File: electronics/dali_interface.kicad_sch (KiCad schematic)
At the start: 34 parts, among them J1 Screw_Terminal_01x04, J4 Conn_01x02, Q1 MMBT5551L, Q2 DMN62D0U, U2 TPS62932

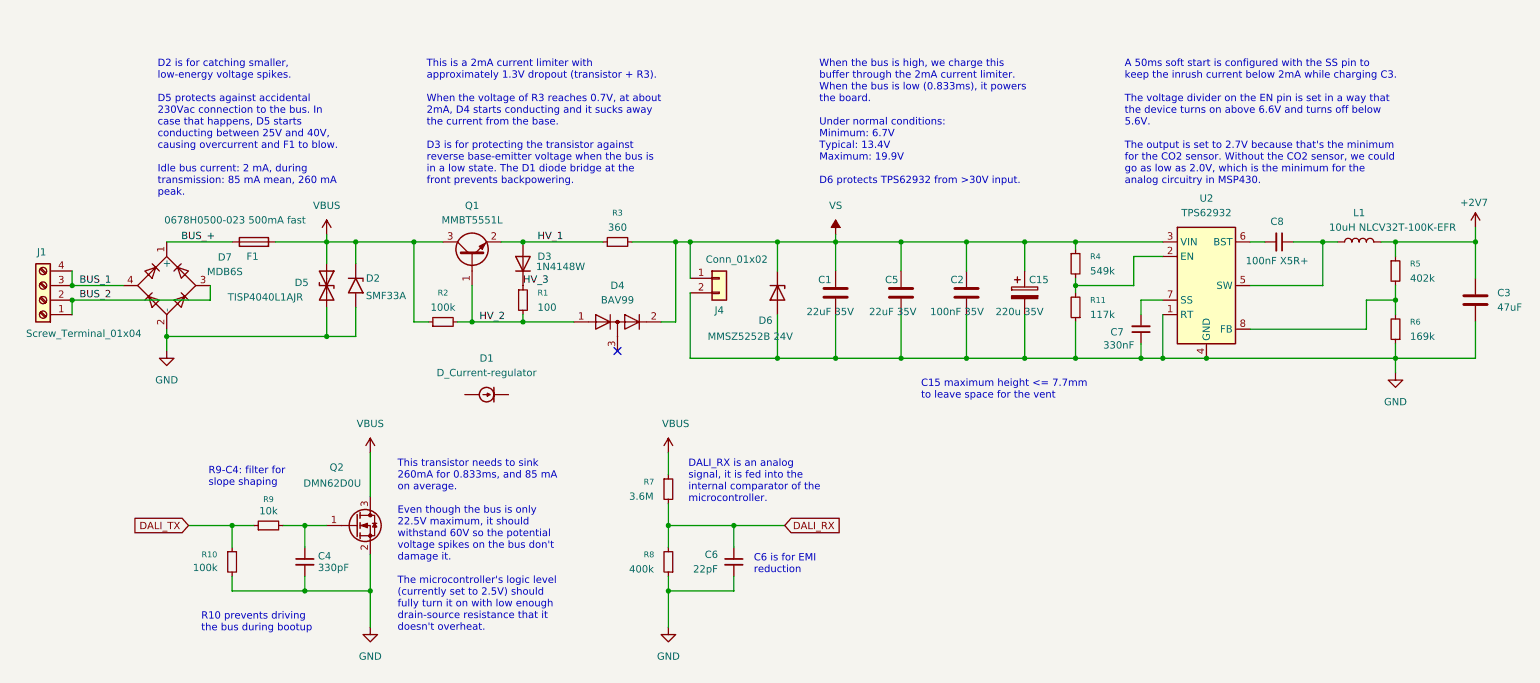
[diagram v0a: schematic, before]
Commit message: Fixed errors of the first hw prototype
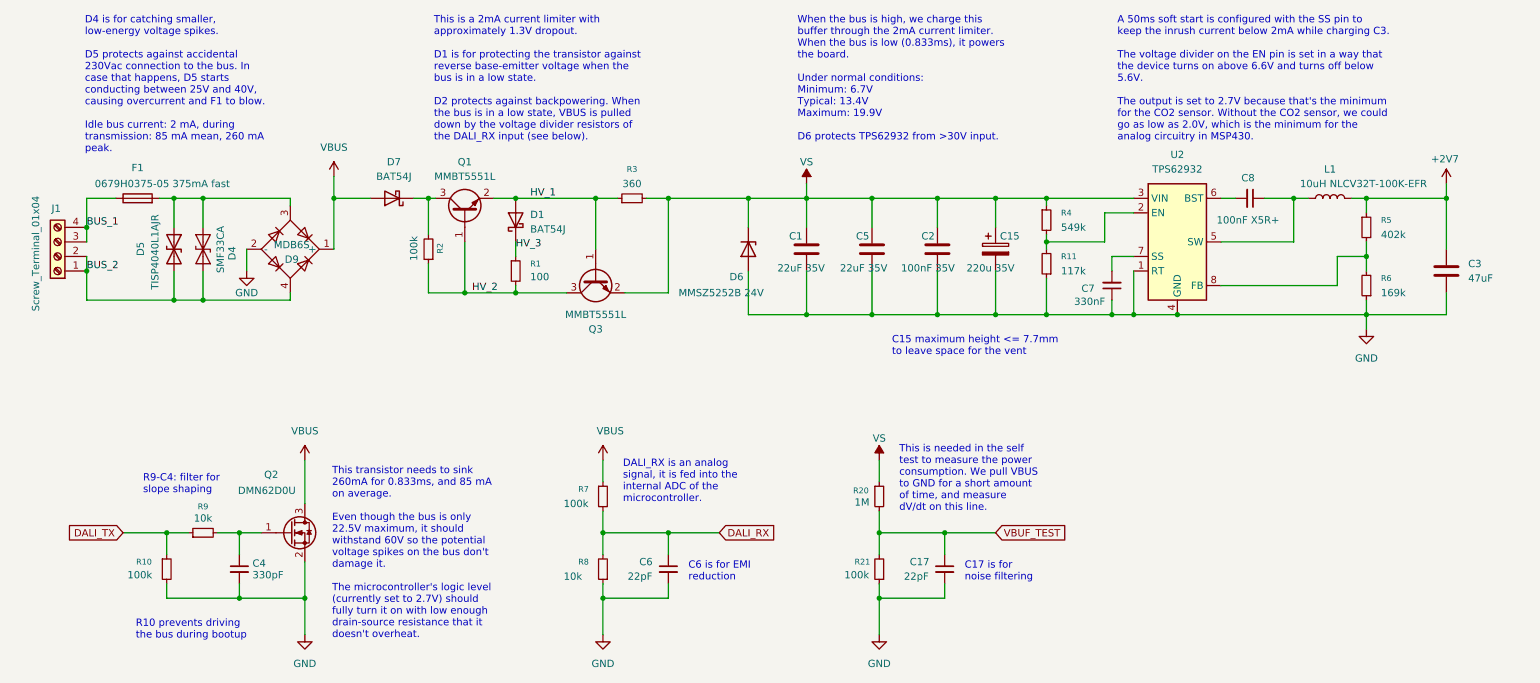
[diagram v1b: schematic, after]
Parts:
- removed D1: D_Current-regulator, Diode_SMD:D_MELF, symbol Device:D_Current-regulator
- removed D2: SMF33A, Diode_SMD:D_SMF-DEBUG, symbol Diode:SMF33A
- removed D3: 1N4148W, Diode_SMD:D_SOD-123, symbol Diode:1N4148W
- removed D4: BAV99, Package_TO_SOT_SMD:SOT-23, symbol Diode:BAV99
- removed D7: MDB6S, Package_SO:TSSOP-4_4.4x5mm_P4mm, symbol Diode_Bridge:MDB6S
- removed J4: Conn_01x02, Connector_PinSocket_1.27mm:PinSocket_1x02_P1.27mm_Vertical, symbol Connector_Generic:Conn_01x02
- added C17: 22pF, Capacitor_SMD:C_0603_1608Metric_Pad1.08x0.95mm_HandSolder, symbol Device:C_Small
- added D1, D7: BAT54J, Diode_SMD:D_SOD-323_HandSoldering, symbol Diode:BAT54J
- added D4: SMF33CA, Diode_SMD:D_SOD-123-DEBUG, symbol Diode:SMAJ33CA
- added D9: MDB6S, Package_SO:TSSOP-4_4.4x5mm_P4mm, symbol Diode_Bridge:MDB6S
- added Q3: MMBT5551L, Package_TO_SOT_SMD:SOT-23, symbol Transistor_BJT:MMBT5551L
- added R20: 1M, Resistor_SMD:R_0603_1608Metric_Pad0.98x0.95mm_HandSolder, symbol Device:R_Small
- added R21: 100k, Resistor_SMD:R_0603_1608Metric_Pad0.98x0.95mm_HandSolder, symbol Device:R_Small
- C15: footprint Capacitor_SMD:CP_Elec_10x7.7 -> Capacitor_SMD:CP_Elec_6.3x7.7
- F1: value 0678H0500-023 500mA fast -> 0679H0375-05 375mA fast
- R3: footprint Resistor_SMD:R_1206_3216Metric_Pad1.30x1.75mm_HandSolder -> Resistor_SMD:R_0603_1608Metric_Pad0.98x0.95mm_HandSolder
- R7: value 3.6M -> 100k
- R8: value 400k -> 10k
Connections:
- net BUS_+ is gone; now on net BUS_1: F1.1
- net BUS_2: now also D5.2 (A2), D4.1 (A1), D9.4
- net GND: now also C17.2, D9.2 (-), R21.1; no longer D5.2 (A2)
- net HV_1: now also D1.2 (A), Q3.1 (B)
- net HV_2: now also R2.1, Q3.3 (C); no longer R2.2
- net HV_3: now also D1.1 (K)
- net VBUS: now also D7.2 (A), D9.1 (+); no longer D5.1 (A1), F1.2, Q1.3 (C), R2.1
- net VS: now also Q3.2 (E), R20.1
- new net: D4.2 (A2), D5.1 (A1), D9.3, F1.2
- new net: D7.1 (K), Q1.3 (C), R2.2
- new net VBUF_TEST: C17.1, R20.2, R21.2
- no-connect marks 1 -> 0
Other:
- moved on the sheet: C1, C15, C2, C3, C4, C5, C6, C7, C8, D5, D6, F1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
